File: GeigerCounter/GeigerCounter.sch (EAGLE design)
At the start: 37 parts, among them IC1 OPAMP-DUALU

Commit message: Beginning to debug errors. Have not poured ground pour yet.
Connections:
- net GND: no longer U$1.MNT1, U$1.MNT2
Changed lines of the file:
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@@
 <net name="GND" class="0">
 <segment>
-<wire x1="441.96" y1="223.52" x2="439.42" y2="223.52" width="0.1524" layer="91"/>
 <pinref part="GND1" gate="1" pin="GND"/>
-<wire x1="439.42" y1="223.52" x2="436.88" y2="223.52" width="0.1524" layer="91"/>
+<wire x1="441.96" y1="223.52" x2="436.88" y2="223.52" width="0.1524" layer="91"/>
 <wire x1="436.88" y1="223.52" x2="431.8" y2="223.52" width="0.1524" layer="91"/>
 <wire x1="431.8" y1="223.52" x2="421.64" y2="223.52" width="0.1524" layer="91"/>
 <wire x1="421.64" y1="223.52" x2="421.64" y2="213.36" width="0.1524" layer="91"/>
 <pinref part="U$1" gate="P$1" pin="6"/>
-<pinref part="U$1" gate="P$1" pin="MNT1"/>
-<wire x1="459.74" y1="215.9" x2="459.74" y2="218.44" width="0.1524" layer="91"/>
-<pinref part="U$1" gate="P$1" pin="MNT2"/>
-<wire x1="457.2" y1="215.9" x2="457.2" y2="218.44" width="0.1524" layer="91"/>
-<wire x1="457.2" y1="215.9" x2="459.74" y2="215.9" width="0.1524" layer="91"/>
-<wire x1="457.2" y1="215.9" x2="439.42" y2="215.9" width="0.1524" layer="91"/>
-<junction x="457.2" y="215.9"/>
-<wire x1="439.42" y1="215.9" x2="439.42" y2="223.52" width="0.1524" layer="91"/>
-<junction x="439.42" y="223.52"/>
 <pinref part="TP_GND" gate="G$1" pin="TP"/>
 <junction x="431.8" y="223.52"/>

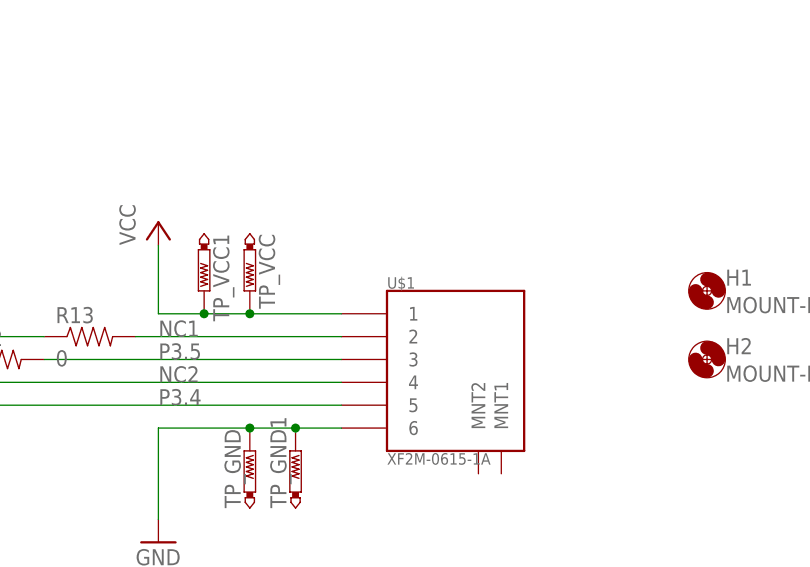
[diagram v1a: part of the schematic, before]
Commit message: Added silkscreen
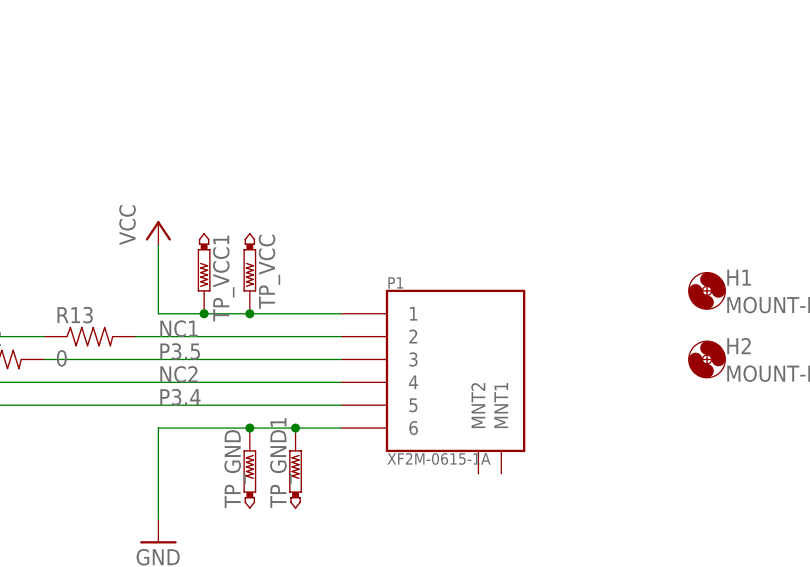
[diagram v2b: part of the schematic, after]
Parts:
- renumbered U$1 to P1
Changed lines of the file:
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@@
 <setting verticaltext="up"/>
 </settings>
-<grid distance="0.1" unitdist="inch" unit="inch" style="lines" multiple="1" display="yes" altdistance="0.01" altunitdist="inch" altunit="inch"/>
+<grid distance="0.1" unitdist="inch" unit="inch" style="lines" multiple="1" display="no" altdistance="0.01" altunitdist="inch" altunit="inch"/>
 <layers>
 <layer number="1" name="Top" color="4" fill="1" visible="no" active="no"/>
@@
 <part name="GND1" library="supply1" deviceset="GND" device=""/>
 <part name="P+1" library="supply1" deviceset="VCC" device=""/>
-<part name="U$1" library="GeigerCounter" deviceset="XF2M-0615-1A" device=""/>
+<part name="P1" library="GeigerCounter" deviceset="XF2M-0615-1A" device=""/>
 <part name="P+2" library="supply1" deviceset="VCC" device=""/>
 <part name="GND2" library="supply1" deviceset="GND" device=""/>
@@
 <instance part="GND1" gate="1" x="421.64" y="210.82"/>
 <instance part="P+1" gate="VCC" x="421.64" y="246.38"/>
-<instance part="U$1" gate="P$1" x="447.04" y="223.52"/>
+<instance part="P1" gate="P$1" x="447.04" y="223.52"/>
 <instance part="P+2" gate="VCC" x="129.54" y="248.92"/>
 <instance part="GND2" gate="1" x="129.54" y="223.52"/>
@@
 <wire x1="421.64" y1="243.84" x2="421.64" y2="236.22" width="0.1524" layer="91"/>
 <wire x1="421.64" y1="236.22" x2="426.72" y2="236.22" width="0.1524" layer="91"/>
-<pinref part="U$1" gate="P$1" pin="1"/>
+<pinref part="P1" gate="P$1" pin="1"/>
 <pinref part="TP_VCC" gate="G$1" pin="TP"/>
 <wire x1="426.72" y1="236.22" x2="431.8" y2="236.22" width="0.1524" layer="91"/>
@@
 <wire x1="431.8" y1="223.52" x2="421.64" y2="223.52" width="0.1524" layer="91"/>
 <wire x1="421.64" y1="223.52" x2="421.64" y2="213.36" width="0.1524" layer="91"/>
-<pinref part="U$1" gate="P$1" pin="6"/>
+<pinref part="P1" gate="P$1" pin="6"/>
 <pinref part="TP_GND" gate="G$1" pin="TP"/>
 <junction x="431.8" y="223.52"/>
@@
 <segment>
 <label x="421.64" y="231.14" size="1.778" layer="95"/>
-<pinref part="U$1" gate="P$1" pin="3"/>
+<pinref part="P1" gate="P$1" pin="3"/>
 <wire x1="408.94" y1="231.14" x2="441.96" y2="231.14" width="0.1524" layer="91"/>
 <pinref part="R12" gate="G$1" pin="2"/>
@@
 <segment>
 <label x="421.64" y="226.06" size="1.778" layer="95"/>
-<pinref part="U$1" gate="P$1" pin="5"/>
+<pinref part="P1" gate="P$1" pin="5"/>
 <pinref part="R15" gate="G$1" pin="2"/>
 <wire x1="388.62" y1="226.06" x2="441.96" y2="226.06" width="0.1524" layer="91"/>
@@
 <net name="NC1" class="0">
 <segment>
-<pinref part="U$1" gate="P$1" pin="2"/>
+<pinref part="P1" gate="P$1" pin="2"/>
 <wire x1="441.96" y1="233.68" x2="419.1" y2="233.68" width="0.1524" layer="91"/>
 <label x="421.64" y="233.68" size="1.778" layer="95"/>
@@
 <net name="NC2" class="0">
 <segment>
-<pinref part="U$1" gate="P$1" pin="4"/>
+<pinref part="P1" gate="P$1" pin="4"/>
 <wire x1="441.96" y1="228.6" x2="398.78" y2="228.6" width="0.1524" layer="91"/>
 <label x="421.64" y="228.6" size="1.778" layer="95"/>

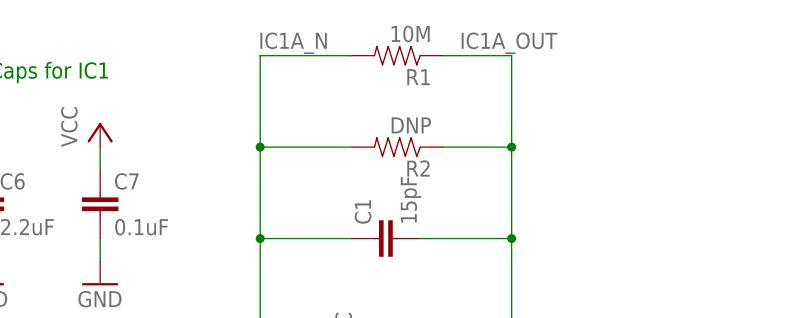
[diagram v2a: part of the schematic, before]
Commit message: Changed the feedback resistor for the first stage amplifier to be 1M instead of 10M. At 10M it was pulling the output low.
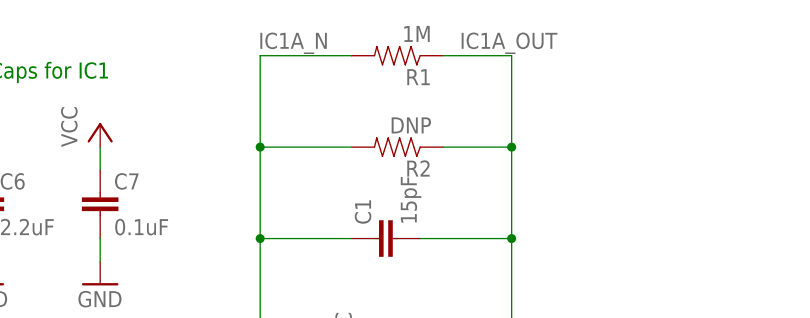
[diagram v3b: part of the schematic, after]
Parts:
- R1: value 10M -> 1M
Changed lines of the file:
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@@
 <part name="C4" library="SparkFun-Passives" deviceset="CAP" device="0603-CAP" value="DNP"/>
 <part name="C5" library="SparkFun-Passives" deviceset="CAP" device="0603-CAP" value="DNP"/>
-<part name="R1" library="SparkFun-Passives" deviceset="RESISTOR" device="0603-RES" value="10M"/>
+<part name="R1" library="SparkFun-Passives" deviceset="RESISTOR" device="0603-RES" value="1M"/>
 <part name="R2" library="SparkFun-Passives" deviceset="RESISTOR" device="0603-RES" value="DNP"/>
 <part name="R3" library="SparkFun-Passives" deviceset="RESISTOR" device="0603-RES" value="0"/>
